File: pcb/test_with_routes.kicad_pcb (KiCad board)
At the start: 4 copper layers, 120 x 170 mm, 33 parts, among them Q1 IKW40N120H3, Q2 IKW40N120H3

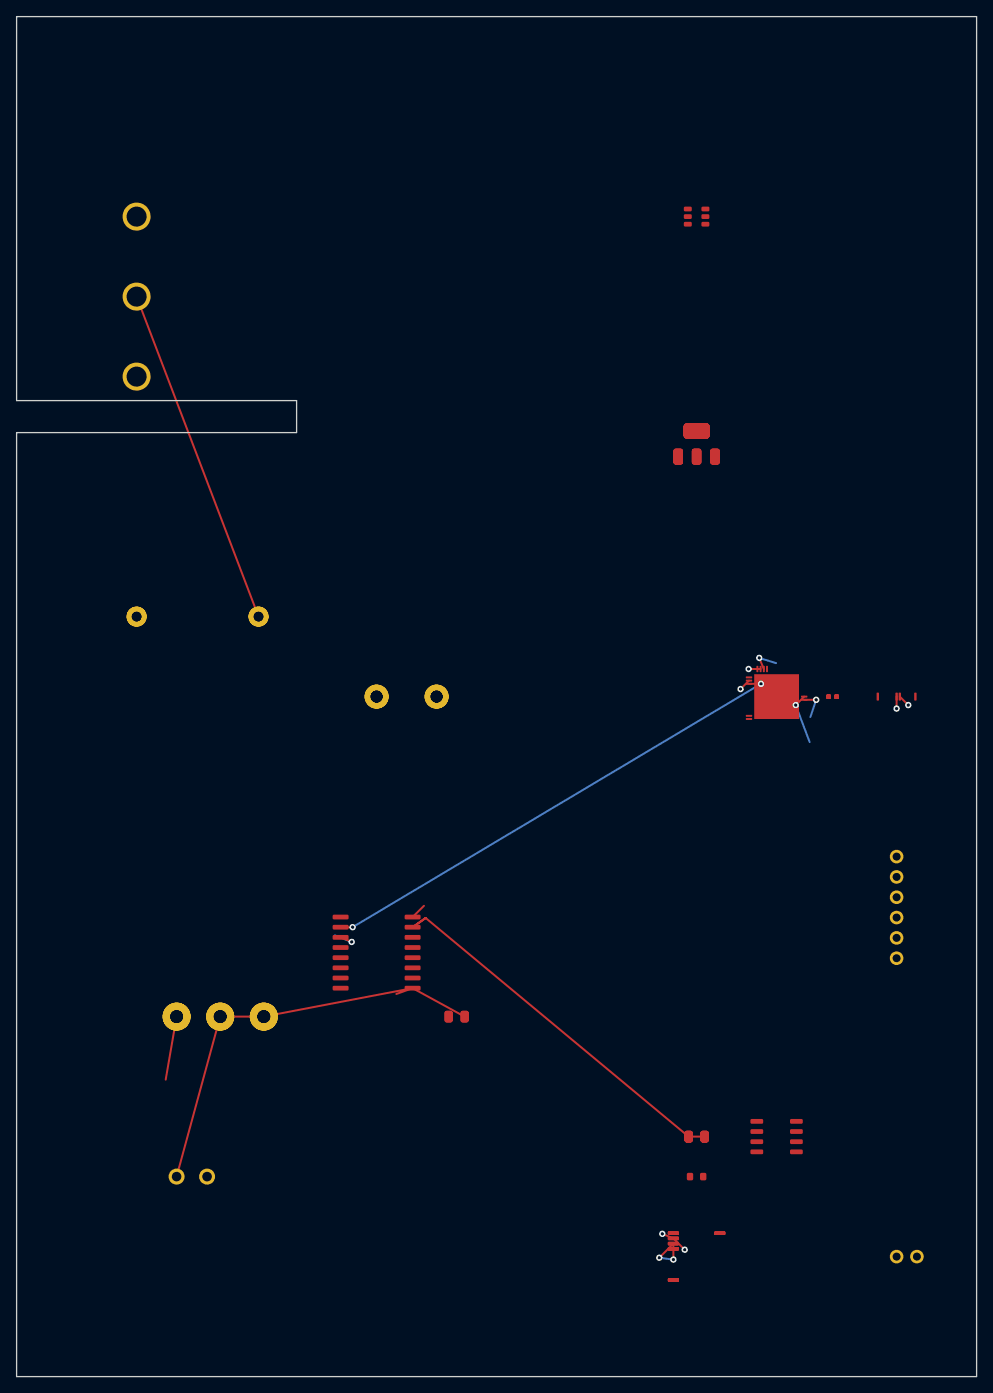
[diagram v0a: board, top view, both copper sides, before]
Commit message: checkpoint: before ExactGeometryRouter Phase 1-3 improvements
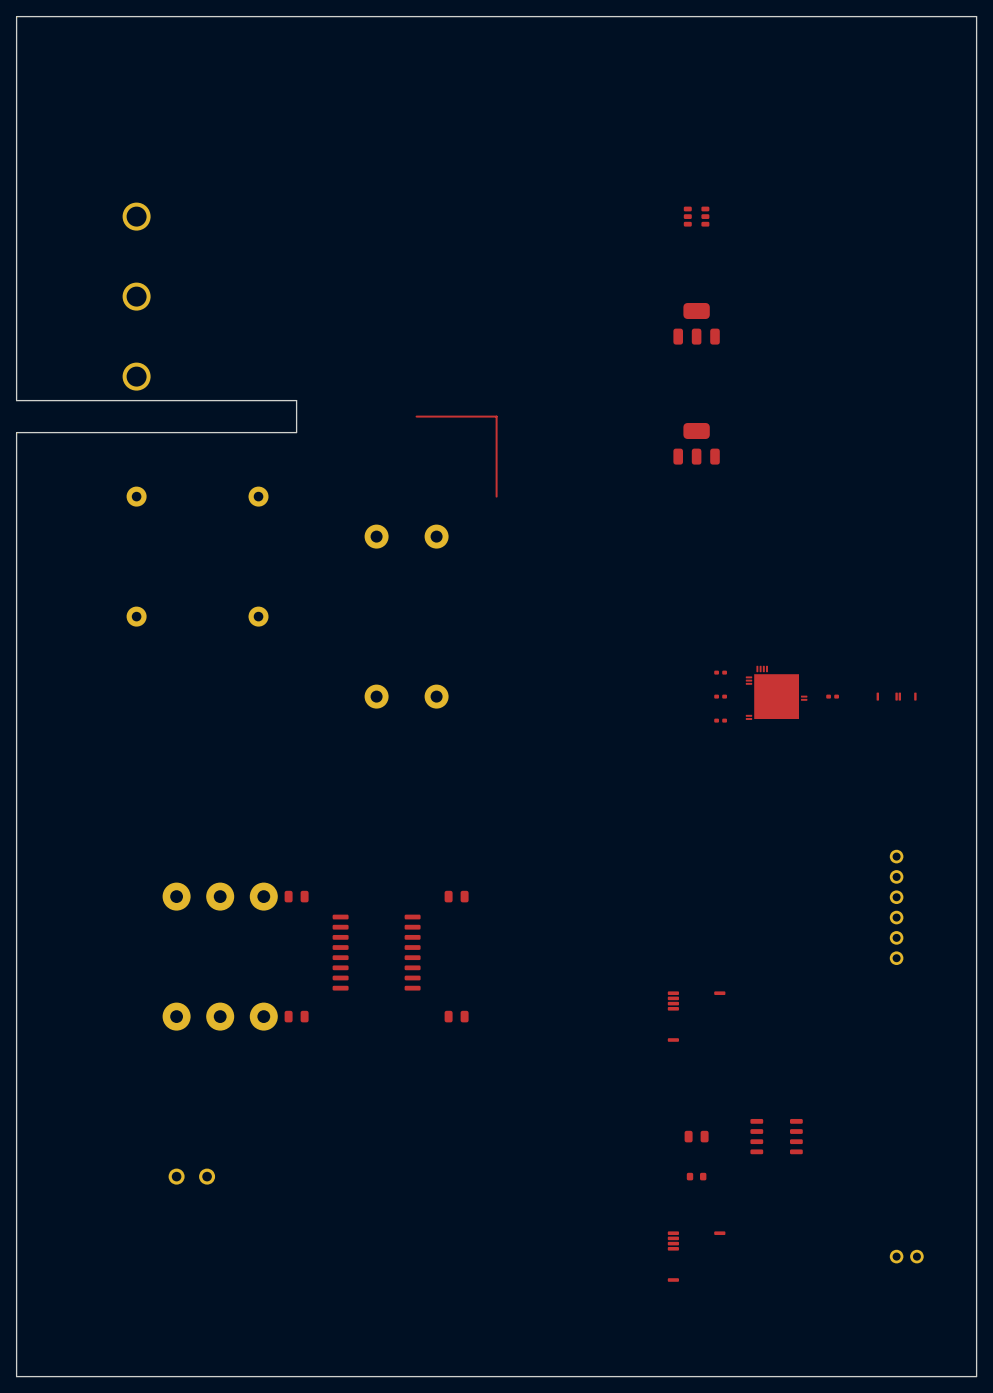
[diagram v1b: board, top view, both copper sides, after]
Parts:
- moved R_GATE_H 58.3 mm to (35.0, 110.0)
- moved R_GATE_L 52.2 mm to (35.0, 125.0)
- moved U_CT 30.0 mm to (85.0, 125.0)
- moved C_BUS1 20.0 mm to (45.0, 65.0)
- moved C_BOOT 15.0 mm to (55.0, 110.0)
- moved D1 15.0 mm to (15.0, 60.0)
- moved Q1 15.0 mm to (20.0, 110.0)
- moved U_LDO_3V3 15.0 mm to (85.0, 40.0)
- moved C_MCU_1 14.3 mm to (88.0, 82.0)
- moved C_MCU_3 14.3 mm to (88.0, 88.0)
- moved C_MCU_2 14.0 mm to (88.0, 85.0)
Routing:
- net PWM_H: track 62.4 -> 0.00 mm, vias 2 -> 0
- net GATE_H: track 56.7 -> 0.00 mm
- net SW_NODE: track 56.7 -> 0.00 mm
- net AC_N: track 42.8 -> 0.00 mm
- net (no net): track 0.00 -> 20.0 mm
- net SPI_MISO: track 9.99 -> 0.00 mm, vias 3 -> 0
- net SPI_MOSI: track 9.28 -> 0.00 mm, vias 3 -> 0
- net USB_D+: track 7.94 -> 0.00 mm, vias 2 -> 0
- net USB_D-: track 5.27 -> 0.00 mm, vias 2 -> 0
- net PWM_L: track 5.27 -> 0.00 mm, vias 2 -> 0
